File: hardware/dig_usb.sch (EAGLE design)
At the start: 156 parts, among them IC1 AT90USB1287-AU, IC202 DS1337S, IC203 MAX487CSA, IC204 74HC166D, IC301 LTV-356T, IC302 LTV-356T, IC303 LTV-356T, IC304 LTV-356T, IC305 LTV-356T, IC306 LTV-356T, IC307 LTV-356T, IC308 LTV-356T, K401 S202S02, K402 S202S02, K403 S202S02, K404 S202S02, K405 S202S02, K406 S202S02, K407 S202S02, K408 S202S02, Q1 16MHz, Q201 32,768kHz, T301 BCR191, T302 BCR191, T303 BCR191, T304 BCR191, T305 BCR191, T306 BCR191, T307 BCR191, T308 BCR191, X101 RIA-73-02, X201 ISP, X202 RIA-73-02, X301 RIA-73-02, X302 RIA-73-02, X303 RIA-73-02, X304 RIA-73-02, X305 RIA-73-02, X401 RIA-73-02, X402 RIA-73-02, X403 RIA-73-02, X404 RIA-73-02, X405 RIA-73-02

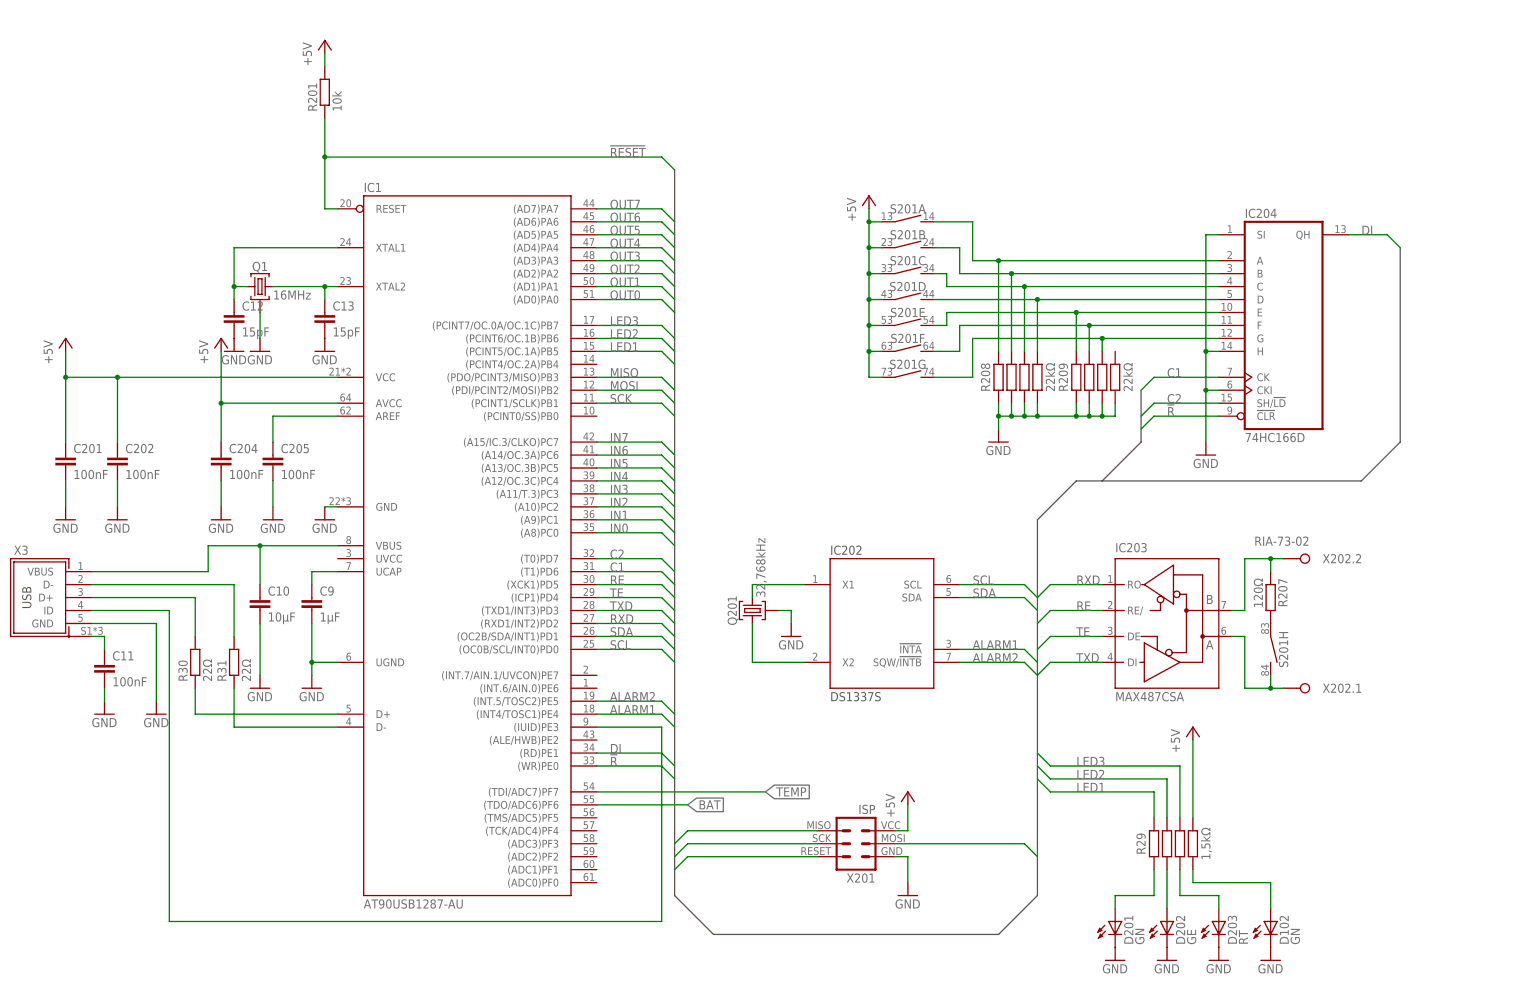
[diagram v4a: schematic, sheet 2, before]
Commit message: dig_usb vorläufig komplett geroutet
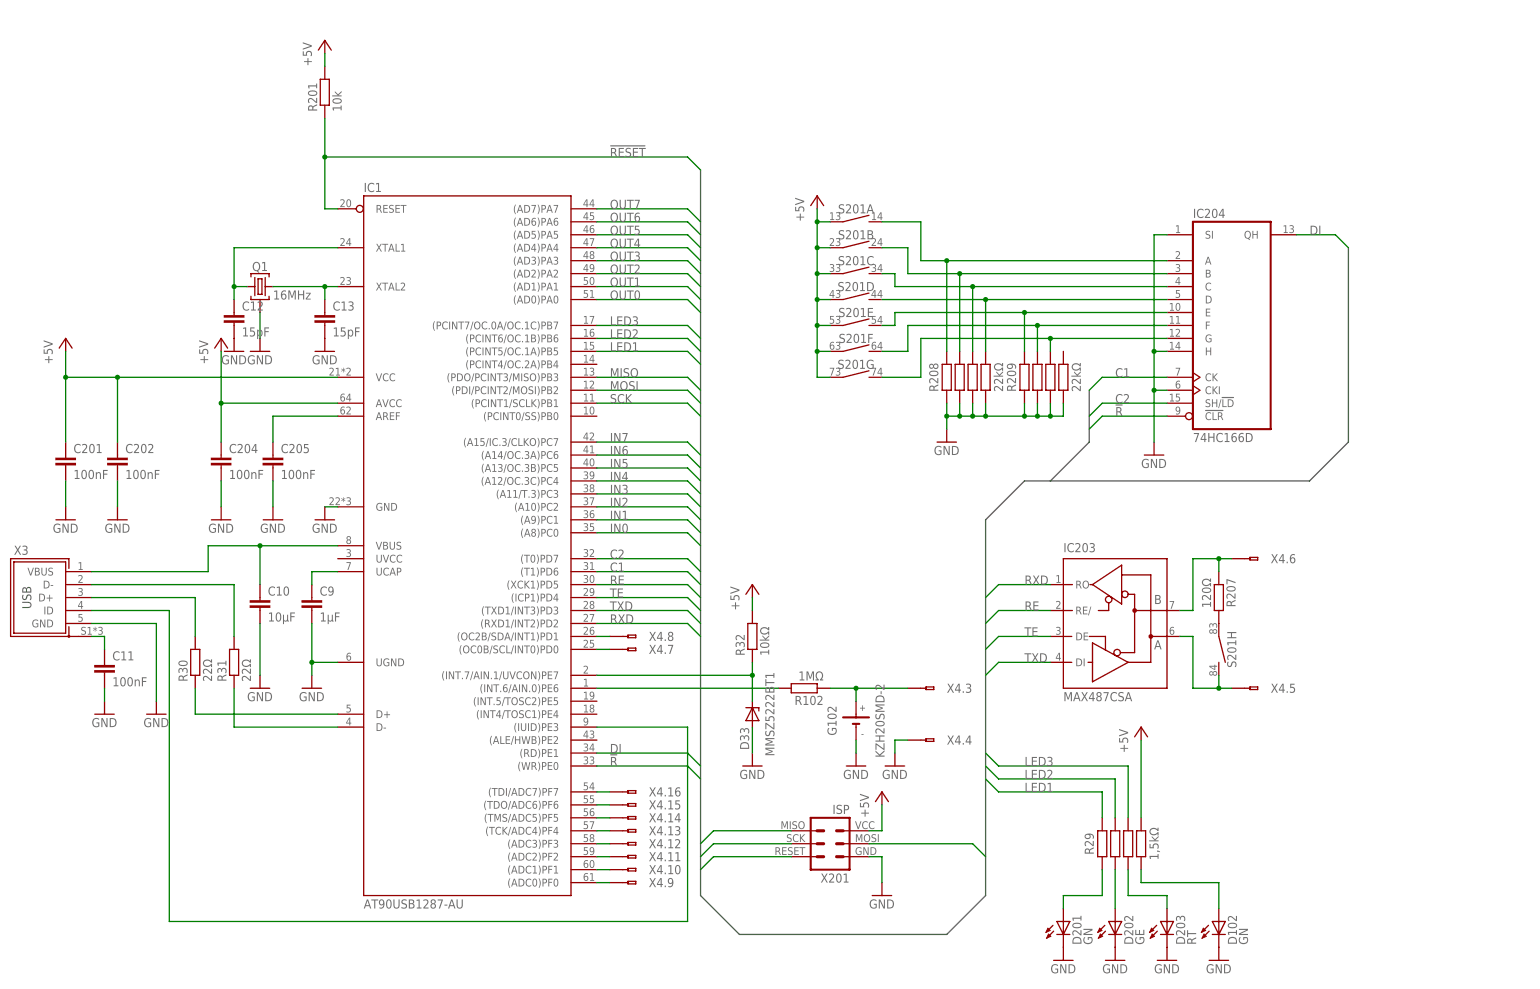
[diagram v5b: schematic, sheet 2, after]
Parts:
- removed R103: 1MΩ, passiv:R_0805
- removed X1: (no value), anschluss:WS20V
- added D33: MMSZ5222BT1, diode:Z-DIODE-SOD123
- added R32: 10kΩ, passiv:R_0805
- added X4: (no value), anschluss:WS34V
- D103, D104: device diode:DIODE-MINIMELF -> diode:DIODE-SOD123
- X2: device anschluss:WS20V -> anschluss:WS34V
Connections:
- removed net ALARM1: IC1.(INT4/TOSC1)PE4, IC202A.!INTA
- removed net ALARM2: IC1.(INT.5/TOSC2)PE5, IC202A.SQW/!INTB
- removed net BAT: IC1.(TDO/ADC6)PF6, R102.1, R103.2
- removed net SCL: IC1.(OC0B/SCL/INT0)PD0, IC202A.SCL
- removed net SDA: IC1.(OC2B/SDA/INT1)PD1, IC202A.SDA
- removed net TEMP: IC1.(TDI/ADC7)PF7, R409.1, R410.1
- new net N$129: D33.K, IC1.(INT.7/AIN.1/UVCON)PE7, R32.1
- new net N$130: D104.A, X2.3.A
- new net N$131: IC202A.SCL, X2.7.A
- new net N$132: IC202A.SDA, X2.8.A
- new net N$133: X2.6.A, X202.2.A
- new net N$134: X2.5.A, X202.1.A
- new net N$135: IC1.(ADC0)PF0, X4.9.A
- new net N$136: IC1.(ADC1)PF1, X4.10.A
- new net N$137: IC1.(ADC2)PF2, X4.11.A
- new net N$138: IC1.(ADC3)PF3, X4.12.A
- new net N$139: IC1.(TCK/ADC4)PF4, X4.13.A
- new net N$140: IC1.(TMS/ADC5)PF5, X4.14.A
- new net N$141: IC1.(TDO/ADC6)PF6, X4.15.A
- new net N$142: IC1.(TDI/ADC7)PF7, X4.16.A
- new net N$143: G102.+, R102.1, X4.3.A
- new net N$144: IC1.(OC0B/SCL/INT0)PD0, X4.7.A
- new net N$145: IC1.(OC2B/SDA/INT1)PD1, X4.8.A
- new net N$146: R409.1, R410.1, X2.9.A
- net +5V: now also R32.2, X2.34.A, X4.1.A, X4.34.A; no longer X1.1.A, X1.20.A, X2.20.A
- net GND: now also D33.A, X2.33.A, X2.4.A, X4.2.A, X4.33.A, X4.4.A; no longer R103.1, X1.19.A, X1.2.A, X2.19.A
- net IN0: now also X4.18.A; no longer X2.4.A
- net IN1: now also X4.20.A; no longer X2.6.A
- net IN2: now also X4.22.A; no longer X2.8.A
- net IN3: now also X4.24.A; no longer X2.10.A
- net IN4: now also X4.26.A; no longer X2.12.A
- net IN5: now also X4.28.A; no longer X2.14.A
- net IN6: now also X4.30.A; no longer X2.16.A
- net IN7: now also X4.32.A; no longer X2.18.A
- net N$100: now also X2.30.A; no longer X1.16.A
- net N$101: now also X2.32.A; no longer X1.18.A
- net N$20: now also X4.5.A; no longer X202.1.A
- net N$21: now also IC1.(INT.6/AIN.0)PE6; no longer D104.A, G102.+
- net N$22: now also X4.6.A; no longer X202.2.A
- net N$67: now also X2.17.A; no longer X1.3.A
- net N$79: now also X2.19.A; no longer X1.5.A
- net N$87: now also X2.21.A; no longer X1.7.A
- net N$88: now also X2.23.A; no longer X1.9.A
- net N$90: now also X2.25.A; no longer X1.11.A
- net N$91: now also X2.27.A; no longer X1.13.A
- net N$92: now also X2.29.A; no longer X1.15.A
- net N$93: now also X2.31.A; no longer X1.17.A
- net N$94: now also X2.18.A; no longer X1.4.A
- net N$95: now also X2.20.A; no longer X1.6.A
- net N$96: now also X2.22.A; no longer X1.8.A
- net N$97: now also X2.24.A; no longer X1.10.A
- net N$98: now also X2.26.A; no longer X1.12.A
- net N$99: now also X2.28.A; no longer X1.14.A
- net OUT0: now also X4.17.A; no longer X2.3.A
- net OUT1: now also X4.19.A; no longer X2.5.A
- net OUT2: now also X4.21.A; no longer X2.7.A
- net OUT3: now also X4.23.A; no longer X2.9.A
- net OUT4: now also X4.25.A; no longer X2.11.A
- net OUT5: now also X4.27.A; no longer X2.13.A
- net OUT6: now also X4.29.A; no longer X2.15.A
- net OUT7: now also X4.31.A; no longer X2.17.A
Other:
- moved on the sheet: D102, D201, D202, D203, IC203, IC204, R207, R208, R209, R29, R409, R410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

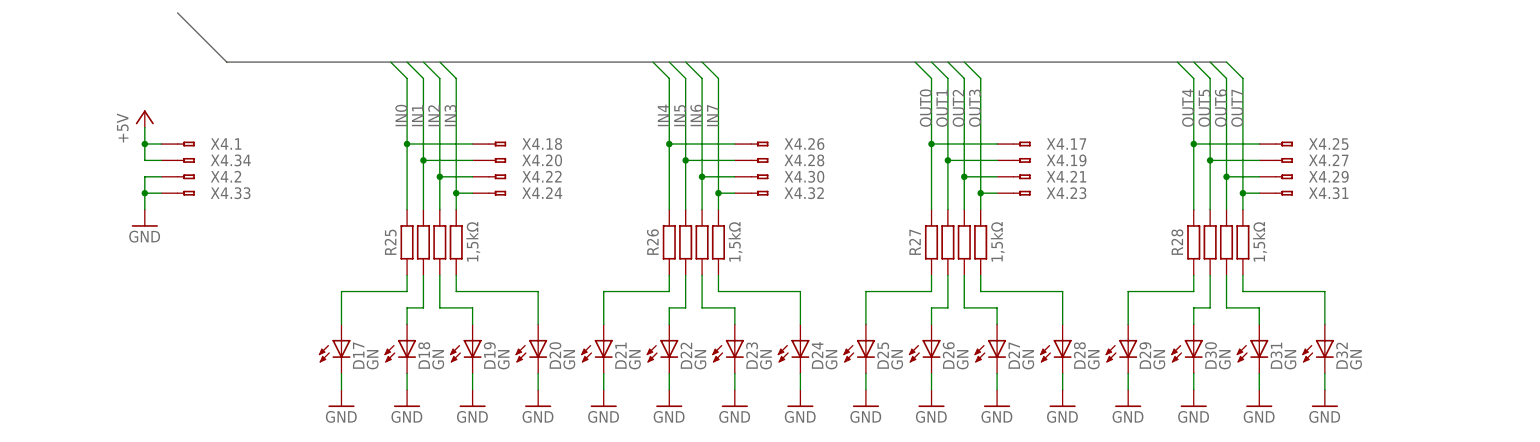
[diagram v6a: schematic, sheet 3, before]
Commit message: Widerstandsarrays für LEDs gegen CHIP0805 bei dig_usb getauscht
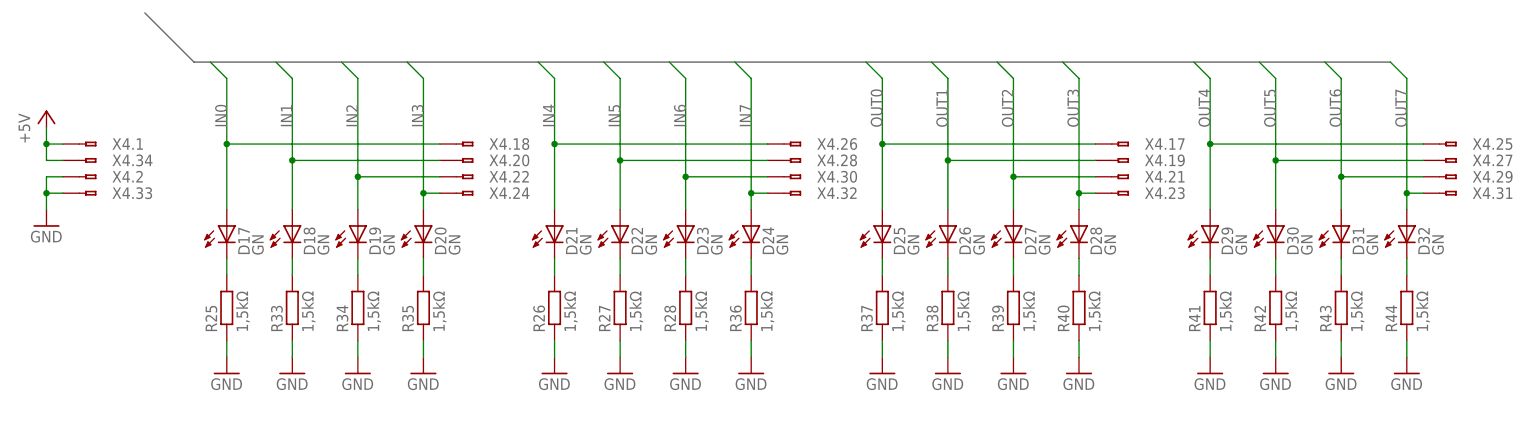
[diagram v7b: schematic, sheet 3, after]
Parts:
- added R33, R34, R35, R36, R37, R38, R39, R40, R41, R42, R43, R44, R45, R46, R47: 1,5kΩ, passiv:R_0805
- R25, R26, R27, R28, R29: device widerstandsnetzwerk:EXB-38V -> passiv:R_0805
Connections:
- net +5V: now also R47.2; no longer R29.8
- net GND: now also R25.1, R26.1, R27.1, R28.1, R33.1, R34.1, R35.1, R36.1, R37.1, R38.1, R39.1, R40.1, R41.1, R42.1, R43.1, R44.1; no longer D17.C, D18.C, D19.C, D20.C, D21.C, D22.C, D23.C, D24.C, D25.C, D26.C, D27.C, D28.C, D29.C, D30.C, D31.C, D32.C
- net IN0: now also D17.A; no longer R25.1
- net IN1: now also D18.A; no longer R25.3
- net IN2: now also D19.A; no longer R25.5
- net IN3: now also D20.A; no longer R25.7
- net IN4: now also D21.A; no longer R26.1
- net IN5: now also D22.A; no longer R26.3
- net IN6: now also D23.A; no longer R26.5
- net IN7: now also D24.A; no longer R26.7
- net LED1: now also R45.2; no longer R29.2
- net LED2: now also R29.2; no longer R29.4
- net LED3: now also R46.2; no longer R29.6
- net N$102: now also D17.C; no longer D17.A
- net N$103: now also D18.C, R33.2; no longer D18.A, R25.4
- net N$104: now also D19.C, R34.2; no longer D19.A, R25.6
- net N$105: now also D20.C, R35.2; no longer D20.A, R25.8
- net N$106: now also D21.C; no longer D21.A
- net N$107: now also D22.C, R27.2; no longer D22.A, R26.4
- net N$108: now also D23.C, R28.2; no longer D23.A, R26.6
- net N$109: now also D24.C, R36.2; no longer D24.A, R26.8
- net N$110: now also D25.C, R37.2; no longer D25.A, R27.1
- net N$111: now also D26.C, R38.2; no longer D26.A, R27.3
- net N$112: now also D27.C, R39.2; no longer D27.A, R27.5
- net N$113: now also D28.C, R40.2; no longer D28.A, R27.7
- net N$114: now also D29.C, R41.2; no longer D29.A, R28.1
- net N$115: now also D30.C, R42.2; no longer D30.A, R28.3
- net N$116: now also D31.C, R43.2; no longer D31.A, R28.5
- net N$117: now also D32.C, R44.2; no longer D32.A, R28.7
- net N$4: now also R46.1; no longer R29.5
- net N$44: now also R47.1; no longer R29.7
- net N$62: now also R45.1; no longer R29.1
- net N$63: now also R29.1; no longer R29.3
- net OUT0: now also D25.A; no longer R27.2
- net OUT1: now also D26.A; no longer R27.4
- net OUT2: now also D27.A; no longer R27.6
- net OUT3: now also D28.A; no longer R27.8
- net OUT4: now also D29.A; no longer R28.2
- net OUT5: now also D30.A; no longer R28.4
- net OUT6: now also D31.A; no longer R28.6
- net OUT7: now also D32.A; no longer R28.8
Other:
- moved on the sheet: D17, D18, D19, D20, D21, D22, D23, D24, D25, D26, D27, D28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

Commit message: CHIP Gehäusebauformen ausgetauscht
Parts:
- D101: value LL5819 -> SD103; device diode:SHOTKY-DIODE-MELF -> diode:SHOTKY-DIODE-SOD123
